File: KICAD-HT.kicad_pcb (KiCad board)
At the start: 4 copper layers, 85 x 70 mm, 147 parts, among them J1 HV_BIAS_IN, J2 DC_HT, Q1 IPD050N10N5, Q2 IPD050N10N5, Q4 MMBF170, Q5 IPD60R360P7, Q6 BSS127I, Q7 BSS127I, T1 MSD1514-103ME, U1 UCC27517, U10 ISO7710, U11 AMC0311R, U12 UCC24612, U13 SN74LVC1G08, U14 TSV791, U15 ATL431, U16 LMV7219, U17 SN74LVC1G132, U18 SN74LVC1G74, U19 ISO7710F, U20 VODA1275, U21 MCP6001, U22 AMC0302R, U3 ISO7710, U5 DPC817, U7 AMC0311R, U9 AMC0302R

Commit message: Via-stitching GND_CTRL (grille 5mm, F.Cu/In1.Cu/B.Cu, 13 vias) ; retrait du via VOUT_N pose au mauvais endroit, methode corrigee documentee
Co-Authored-By: Claude Sonnet 5 <noreply@anthropic.com>
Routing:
- net GND_CTRL: vias 0 -> 13
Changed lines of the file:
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@@
 		(net "3V3_ISO")
 	)
+	(via
+		(at 105 80)
+		(size 0.6)
+		(drill 0.3)
+		(layers "F.Cu" "B.Cu")
+		(net "GND_CTRL")
+	)
+	(via
+		(at 100 110)
+		(size 0.6)
+		(drill 0.3)
+		(layers "F.Cu" "B.Cu")
+		(net "GND_CTRL")
+	)
+	(via
+		(at 100 55)
+		(size 0.6)
+		(drill 0.3)
+		(layers "F.Cu" "B.Cu")
+		(net "GND_CTRL")
+	)
+	(via
+		(at 110 115)
+		(size 0.6)
+		(drill 0.3)
+		(layers "F.Cu" "B.Cu")
+		(net "GND_CTRL")
+	)
+	(via
+		(at 105 60)
+		(size 0.6)
+		(drill 0.3)
+		(layers "F.Cu" "B.Cu")
+		(net "GND_CTRL")
+	)
+	(via
+		(at 110 80)
+		(size 0.6)
+		(drill 0.3)
+		(layers "F.Cu" "B.Cu")
+		(net "GND_CTRL")
+	)
+	(via
+		(at 100 115)
+		(size 0.6)
+		(drill 0.3)
+		(layers "F.Cu" "B.Cu")
+		(net "GND_CTRL")
+	)
+	(via
+		(at 105 115)
+		(size 0.6)
+		(drill 0.3)
+		(layers "F.Cu" "B.Cu")
+		(net "GND_CTRL")
+	)
+	(via
+		(at 105 110)
+		(size 0.6)
+		(drill 0.3)
+		(layers "F.Cu" "B.Cu")
+		(net "GND_CTRL")
+	)
+	(via
+		(at 100 100)
+		(size 0.6)
+		(drill 0.3)
+		(layers "F.Cu" "B.Cu")
+		(net "GND_CTRL")
+	)
+	(via
+		(at 105 75)
+		(size 0.6)
+		(drill 0.3)
+		(layers "F.Cu" "B.Cu")
+		(net "GND_CTRL")
+	)
+	(via
+		(at 100 105)
+		(size 0.6)
+		(drill 0.3)
+		(layers "F.Cu" "B.Cu")
+		(net "GND_CTRL")
+	)
+	(via
+		(at 110 70)
+		(size 0.6)
+		(drill 0.3)
+		(layers "F.Cu" "B.Cu")
+		(net "GND_CTRL")
+	)
 	(segment
 		(start 111.2375 54.237)
@@
 	)
 	(group "Vbias_adc"
-		(members "1e0337e1-3a4d-4ecf-aa98-c84705be21a8" "24149d7b-49a6-4d20-8b09-a2bf9ebe172f"
+		(members "17cd0cb3-58ca-4cae-8f04-0dcfe76948d1" "1e0337e1-3a4d-4ecf-aa98-c84705be21a8"
+			"24149d7b-49a6-4d20-8b09-a2bf9ebe172f" "24de7965-a533-41e3-9aea-c8a2a1b5389e"
 			"2521c220-f9bb-4130-8bdc-8106b85a89af" "26862303-8ed3-4045-bd0e-c2c09112dc44"
 			"2b5b5668-53ee-4a87-9050-27c858f80fb8" "3b513a5b-388f-4312-a199-2e4c30c0a33d"
 			"3b806dbc-990f-4c55-b28f-127423dc7d77" "4277c03e-cc19-4a67-afa7-6b06c1f2b5fa"
 			"49ac21d8-9749-4996-adf0-3a6e0cfba5a4" "4c0f3fdf-921d-487d-b8b0-66dd6d8f0bce"
-			"5ae8fcdd-bb5e-411e-a4c9-ed36394b5e02" "5eaa6b04-7965-4e22-ae13-578e6d361008"
+			"5298483a-86cb-4b8f-b5b0-9b7362c51759" "5997aba6-1121-4a07-9750-373708341eb9"
+			"5ae8fcdd-bb5e-411e-a4c9-ed36394b5e02" "5b4ff941-2716-41a5-851a-880e081d4191"
+			"5eaa6b04-7965-4e22-ae13-578e6d361008" "5ee503bd-706e-47c8-816c-5698754d7e7e"
 			"65ebad88-ea5e-4d41-ba87-319c4a75b3ab" "6c8d5106-dbe5-406a-85c4-500bc469309a"
-			"74b53d04-ec0c-4b35-af2d-ca42771ca719" "7ea8221a-4760-448d-9443-f1c977ab9eaa"
+			"71630b95-3479-47af-9b44-ba41fc16ad05" "74b53d04-ec0c-4b35-af2d-ca42771ca719"
+			"7ea8221a-4760-448d-9443-f1c977ab9eaa" "7f95be9e-8637-492d-84a0-c90a98d7848d"
 			"811099c4-859e-412e-8687-c3439a16dac7" "8f3002cb-7bf7-4a56-be5b-1b39a2a17df3"
-			"9be34025-7ee3-4d85-b229-f348c98df5d2" "a2b5893d-042c-457e-bffd-20ae3e9448e5"
-			"a4c7f6df-d193-49d2-9c50-baafcec532d3" "b2d8e595-a160-422d-87e5-7224ab550c19"
-			"ba94c3d3-52d9-411d-8f34-8a9335e2e46b" "bca5d8c2-b396-4f83-a547-88039c377914"
-			"d0233994-96ba-4afb-a086-b49560f87456" "d695894e-4973-4987-a18e-a934871cb343"
-			"e520675b-69b9-4969-a81b-1a68f4750c36" "e5917e14-c314-4217-ad6a-fe292a06f1b3"
-			"e6abc1e0-836e-4300-98b6-831c6c14afce" "ed0924ba-0249-4481-bc59-8f9298b6efa7"
-			"f3c2160d-0973-4d8b-9184-46b245972c76" "fc284748-3f52-4673-940e-fde0f62532b8"
+			"9855f9e3-5db7-41fc-94f1-137a9abd6afa" "9be34025-7ee3-4d85-b229-f348c98df5d2"
+			"a2b5893d-042c-457e-bffd-20ae3e9448e5" "a4c7f6df-d193-49d2-9c50-baafcec532d3"
+			"a831e526-d576-4654-bfd5-edb1c4072029" "b074932d-a434-4945-8539-c91be1879b66"
+			"b2d8e595-a160-422d-87e5-7224ab550c19" "ba94c3d3-52d9-411d-8f34-8a9335e2e46b"
+			"bca5d8c2-b396-4f83-a547-88039c377914" "d0233994-96ba-4afb-a086-b49560f87456"
+			"d624b88a-4066-41b6-8455-1ef682680dbc" "d695894e-4973-4987-a18e-a934871cb343"
+			"da0c52ea-a107-41dc-b90d-f883f33af0d6" "e520675b-69b9-4969-a81b-1a68f4750c36"
+			"e5917e14-c314-4217-ad6a-fe292a06f1b3" "e6abc1e0-836e-4300-98b6-831c6c14afce"
+			"ed0924ba-0249-4481-bc59-8f9298b6efa7" "f3c2160d-0973-4d8b-9184-46b245972c76"
+			"fc284748-3f52-4673-940e-fde0f62532b8"
 		)
 	)

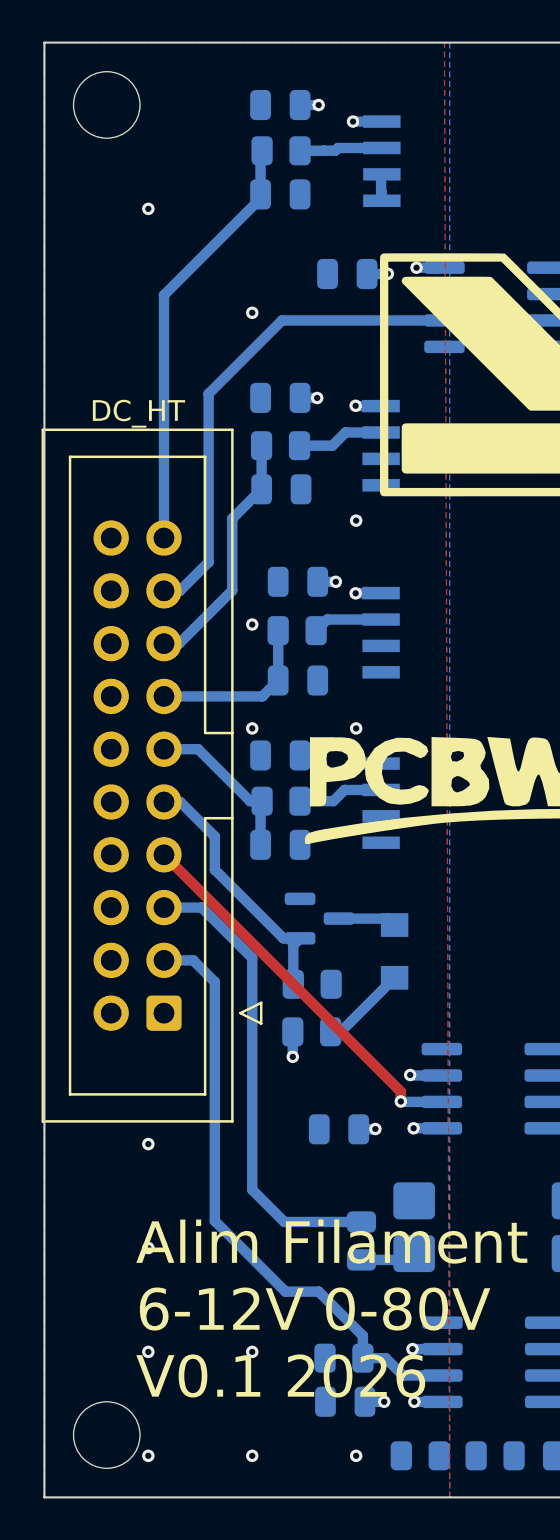
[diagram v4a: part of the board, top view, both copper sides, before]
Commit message: Via-stitching GND_CTRL : grille ancree 1mm du bord reel (pas des coordonnees rondes), 31 vias/5mm puis 52 vias/4mm sur demande
Co-Authored-By: Claude Sonnet 5 <noreply@anthropic.com>
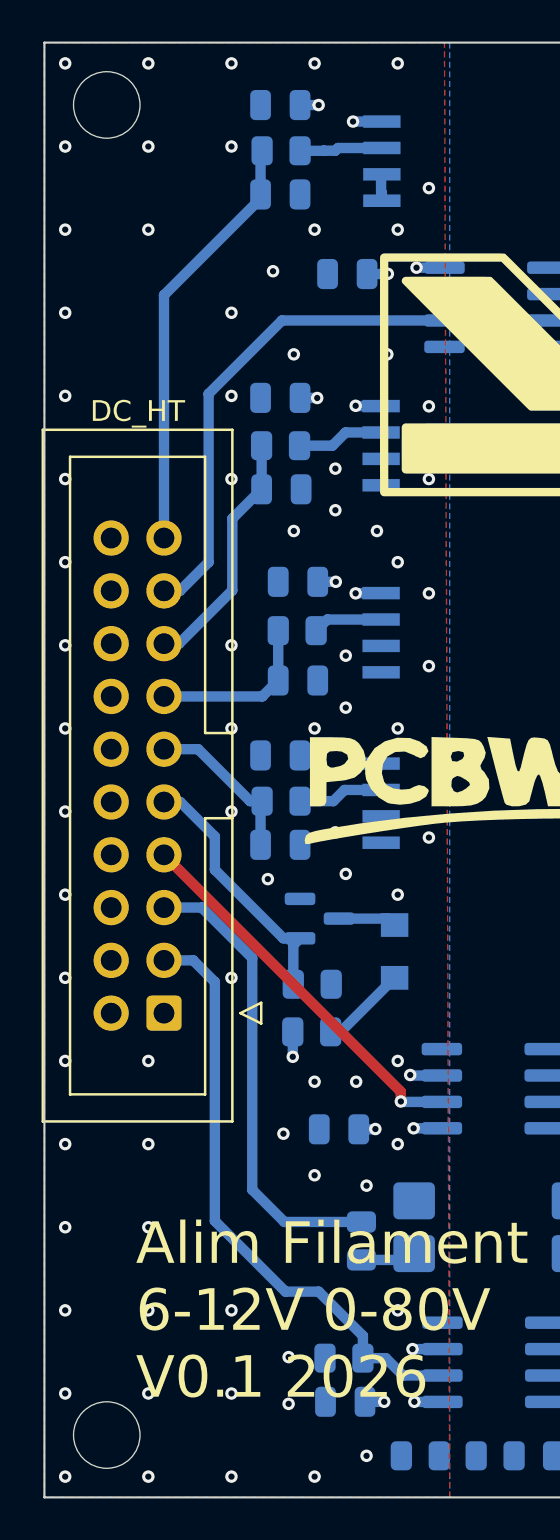
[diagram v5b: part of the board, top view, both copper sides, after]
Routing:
- net GND_CTRL: vias 13 -> 77

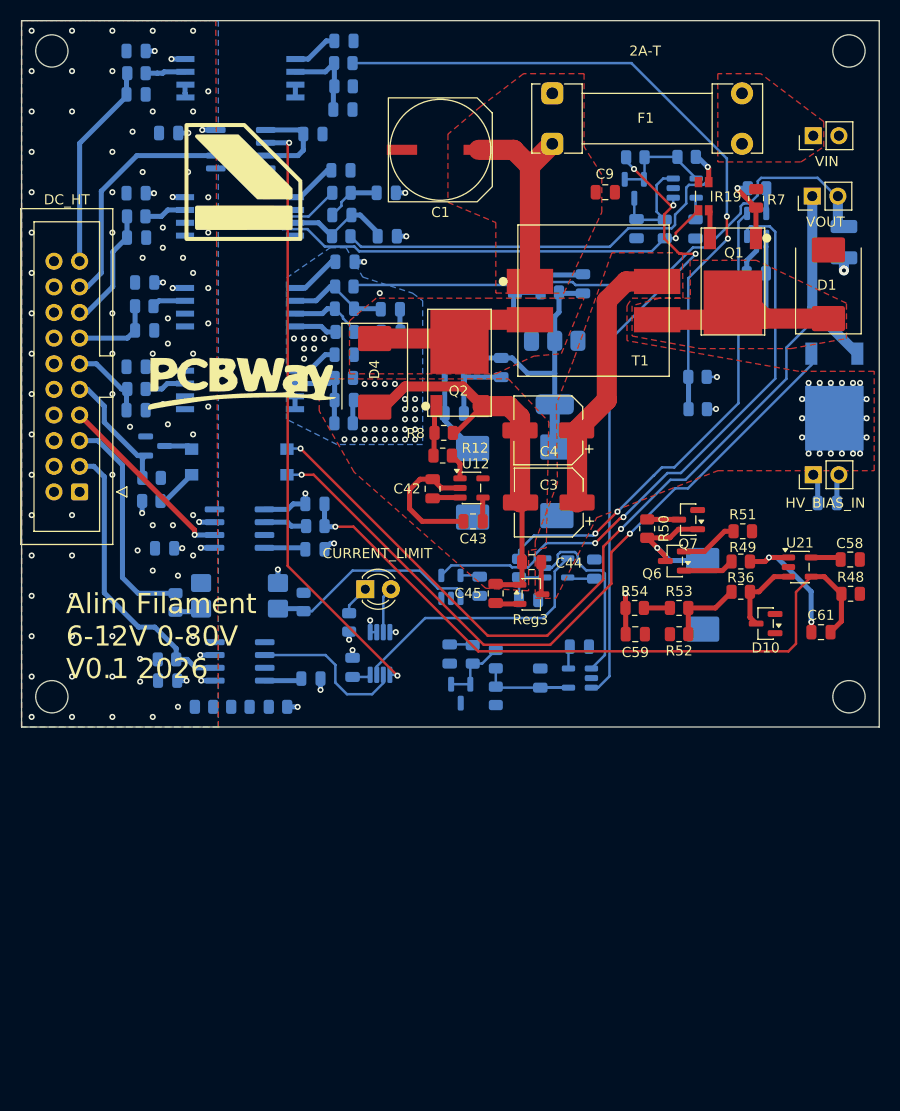
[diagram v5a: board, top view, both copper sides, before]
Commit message: Vias manuels ajoutes dans les zones a forte densite de connexions
Co-Authored-By: Claude Sonnet 5 <noreply@anthropic.com>
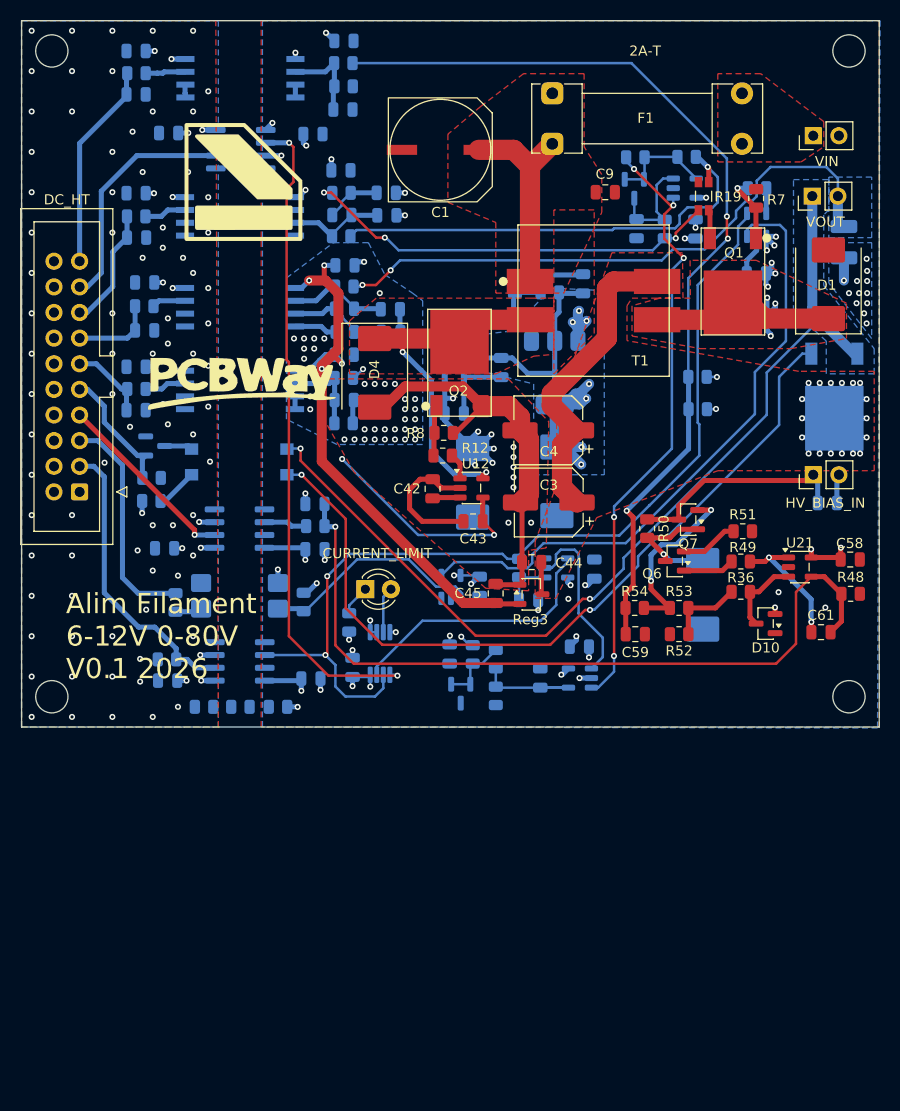
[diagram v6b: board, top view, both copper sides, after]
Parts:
- moved C66 2.07 mm to (131.2, 66.3)
- moved C37 0.36 mm to (127.0, 71.2)
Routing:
- net RAIL_3V3_SEC: track 12.1 -> 58.6 mm, vias 0 -> 4
- net VOUT_P: track 39.1 -> 74.5 mm, vias 19 -> 22
- net PWM_PRI_OUT: track 63.4 -> 92.8 mm
- net HV_BIAS_OUT: track 71.6 -> 93.0 mm
- net SW_SEC: track 16.4 -> 36.0 mm, vias 0 -> 2
- net RAIL_8V25: track 37.0 -> 55.1 mm, vias 0 -> 13
- net HV_BIAS_IN: track 6.12 -> 22.1 mm
- net Net-(Q7-S): track 2.57 -> 17.7 mm, vias 0 -> 2
- net RAIL_3V3_PRI: track 50.9 -> 61.9 mm, vias 0 -> 31
- net ISNS_KP: track 51.3 -> 42.3 mm, vias 1 -> 3
- net VAR_GATE: track 69.6 -> 77.5 mm
- net VIN: track 20.3 -> 27.7 mm, vias 0 -> 3
- net U15_OUTP: track 73.4 -> 79.4 mm
- net ~{Q_TRIP}: track 60.5 -> 64.9 mm
- net EN_PRI_GATED: track 60.0 -> 63.1 mm, vias 2 -> 0
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- added copper zone on B.Cu, net GND
- added copper zone on F.Cu, net GND
- added copper zone on B.Cu, net ISNS_P
- added copper zone on In2.Cu, net RAIL_3V3_PRI
- added copper zone on In2.Cu, net RAIL_3V3_SEC
- added copper zone on B.Cu, net RAIL_8V25
- added copper zone on In2.Cu, net RAIL_8V25
- added copper zone on B.Cu, net V_HT_OUT

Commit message: Via-stitching GND sur toute la carte : grille 4mm ancree a 2mm du bord reel (Edge.Cuts, cote x180), 36 vias
Co-Authored-By: Claude Sonnet 5 <noreply@anthropic.com>
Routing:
- net GND: vias 18 -> 54
